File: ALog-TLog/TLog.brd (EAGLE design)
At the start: 124.1 x 45.3 mm, 94 parts, among them IC1 ATMEGA644M, J6 5.5x2.1mm Barrel, Q1 MOSFET-NCH-BSS138, Q5 MOSFET_PCH-IRLML2244, Q6 MOSFET_PCH-IRLML2244, Q7 MOSFET_PCH-IRLML2244, Q8 MOSFET-NCH-BSS138, Q9 MOSFET-NCH-BSS138, U2 FT231X-Q, U3 915MHz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

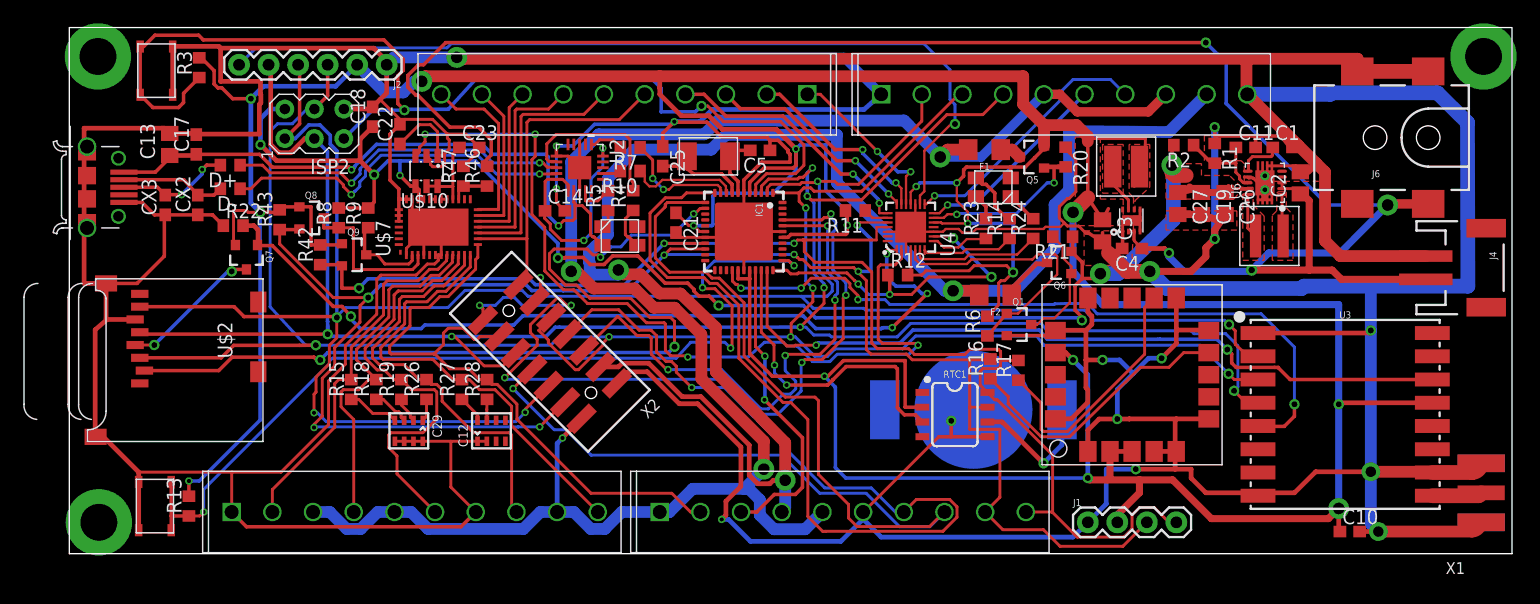
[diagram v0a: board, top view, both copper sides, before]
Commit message: Changes from round #1 of board testing
Changed capacitor sizes, fixed ADC COM pin, fixed DTR pin, connected 5V and VUSB, put converters in series, changed resistor divider values for switchmode regulator
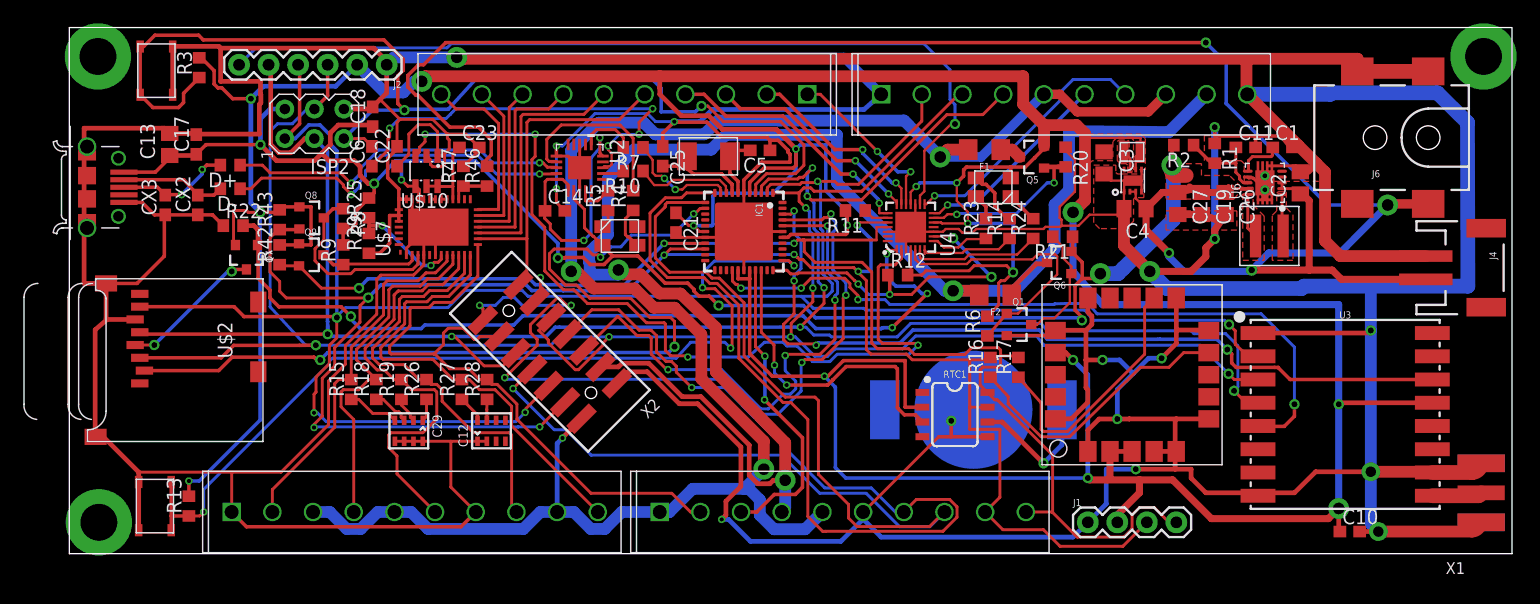
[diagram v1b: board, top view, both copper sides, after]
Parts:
- added C6: 0.1uF, bschulz:C0603
- added R25, R29: 10k, bschulz:R0603
- C4: device bschulz:C0603 -> bschulz:C0805
- L2: value 10uH -> 2.2uF; device bschulz:WE-LQS(4X4) -> bschulz:0806
- R1: value 143k -> 111k
- R2: value 953k -> 1M
- moved C3 5.84 mm to (89.2, 33.7)
- moved R9 3.84 mm to (23.7, 25.8)
- moved Q9 3.68 mm to (20.9, 25.8)
- moved R42 3.49 mm to (18.2, 25.8)
- moved C4 3.44 mm to (91.8, 29.8)
- moved U$4 3.43 mm to (91.6, 32.2)
- moved C22 1.92 mm to (28.3, 34.3)
- moved L2 1.37 mm to (91.6, 34.7)
- moved R8 0.39 mm to (23.7, 28.9), turned to 270 degrees
- moved R17 0.25 mm to (81.8, 16.1)
- moved R10 0.25 mm to (48.6, 33.0)
- moved R7 0.25 mm to (48.6, 35.1)
- moved R16 0.13 mm to (79.4, 16.1)
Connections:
- removed net VUSB: C13.1, C17.1, MICRO_USB.1, U$16.2, U2.12
- new net COM: R25.1, R29.2, U$7.7
- net 5V: now also C13.1, C17.1, C4.1, MICRO_USB.1, R25.2, U$16.2, U$4.2, U$4.3, U2.12
- net BATT+: no longer C4.1, U$4.2, U$4.3
- net DTR: now also C6.1
- net GND: now also R29.1; no longer U$7.7
- net RADIO_INT: now also IC1.42; no longer IC1.32
- net RST: now also C6.2
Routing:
- net VUSB: track 54.4 -> 0.00 mm, vias 2 -> 0
- net 5V: track 132.2 -> 176.4 mm, vias 8 -> 9
- net DTR: track 0.00 -> 35.6 mm, vias 0 -> 4
- net BATT+: track 161.4 -> 148.2 mm, vias 4 -> 3
- net COM: track 0.00 -> 9.61 mm, vias 0 -> 2
- net 3V3: track 429.8 -> 423.5 mm
- net RADIO_INT: track 65.9 -> 72.1 mm, vias 2 -> 4
- net GND: track 841.8 -> 847.5 mm
- net SDA: track 156.7 -> 160.0 mm
- net SDA_HV: track 13.5 -> 16.4 mm
- net RST: track 93.1 -> 95.8 mm
- net SCL: track 121.8 -> 124.3 mm
- net N$2: track 4.25 -> 1.75 mm
- net N$22: track 6.25 -> 8.31 mm
- net SD_VCC_CTRL: track 73.0 -> 75.0 mm
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
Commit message: Fixed Switchmode Converter Errors
Attempted to fix problems with switchmode 5v convetred by adding bottom layer ground plane, and generally improving top planes. In order to attempt to improve overall noise, analog plane was added. Also added control for PSYNC line on 5v converter to GPIO on IO expander
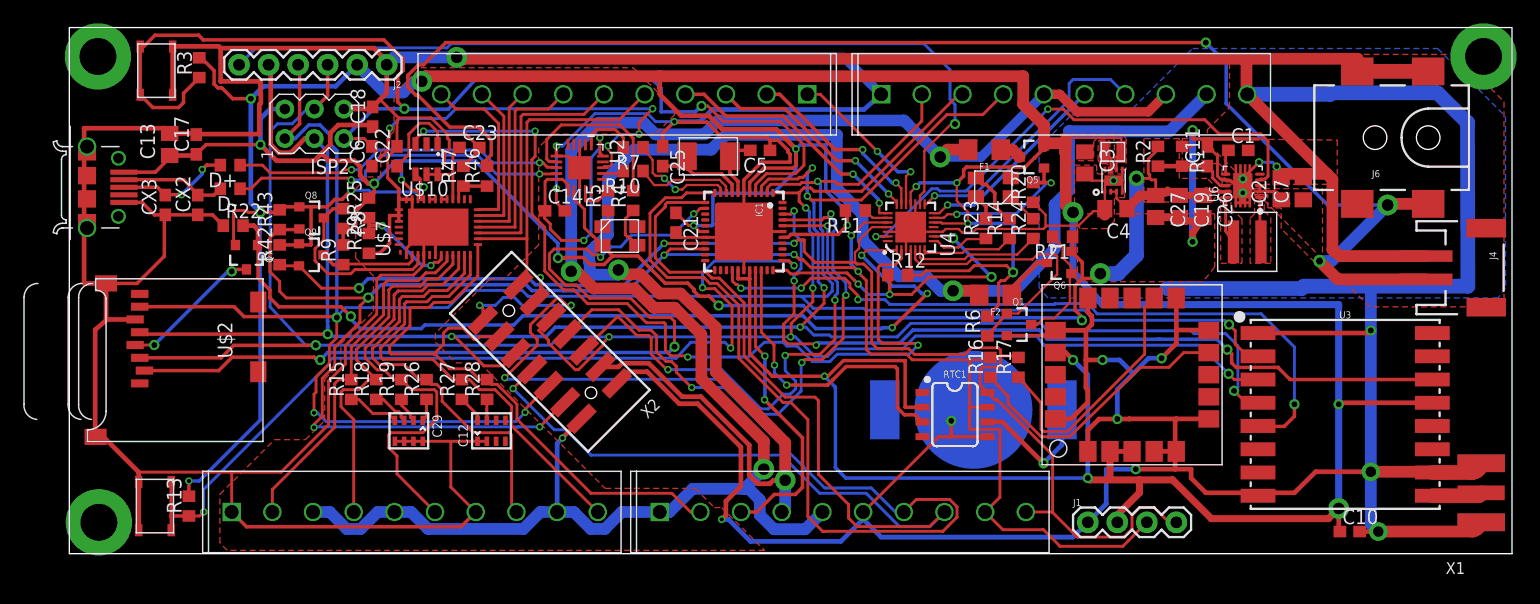
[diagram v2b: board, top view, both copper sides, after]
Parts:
- added C7: 10uF, bschulz:C0805
- moved R20 4.13 mm to (83.1, 31.2), turned to 90 degrees
- moved C1 3.82 mm to (100.7, 34.8)
- moved C11 3.39 mm to (98.0, 34.3), turned to 90 degrees
- moved R1 2.81 mm to (95.9, 34.3)
- moved R2 2.42 mm to (93.8, 34.3), turned to 90 degrees
- moved U$8 1.97 mm to (101.5, 26.9)
- moved C19 1.92 mm to (95.6, 30.0)
- moved C26 1.92 mm to (97.7, 30.0)
- moved C27 1.92 mm to (93.6, 30.0)
- moved U6 1.92 mm to (101.1, 31.8)
- moved C2 1.73 mm to (104.4, 31.5)
- moved C3 1.65 mm to (87.5, 33.7)
- moved C4 1.65 mm to (90.2, 29.8)
- moved L2 1.65 mm to (89.9, 34.7)
- moved U$4 1.65 mm to (90.0, 32.2)
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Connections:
- removed net BATT+: C2.1, J4.2, J6.VIN0, R46.2, U6.2, U6.3
- new net 5V_PSYNC: U4.27, U6.4
- new net BATT: C2.1, C7.1, J4.2, J6.VIN0, R46.2, U6.2, U6.3
- net 3V3: now also U$10.4
- net 5V: no longer U$10.4
- net GND: now also C7.2; no longer U6.4
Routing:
- net BATT+: track 148.2 -> 0.00 mm, vias 3 -> 0
- net BATT: track 0.00 -> 130.7 mm, vias 0 -> 3
- net 5V_PSYNC: track 0.00 -> 44.5 mm, vias 0 -> 2
- net GND: track 847.5 -> 830.9 mm, vias 16 -> 18
- net 5V: track 176.4 -> 161.9 mm, vias 9 -> 8
- net 3V3: track 423.5 -> 431.4 mm, vias 17 -> 19
- net SCL: track 124.3 -> 121.0 mm
- net SD_VCC_CTRL: track 75.0 -> 77.9 mm
- net N$4: track 3.87 -> 2.24 mm
- net EXT_5V: track 138.6 -> 140.1 mm
- net SDA: track 160.0 -> 158.7 mm
- net N$46: track 30.9 -> 29.6 mm
- net N$6: track 7.97 -> 6.86 mm
- net N$38: track 30.3 -> 29.2 mm
- net N$22: track 8.31 -> 7.40 mm
- added copper zone on layer 1, net BATT
- added copper zone on layer 16, net GND

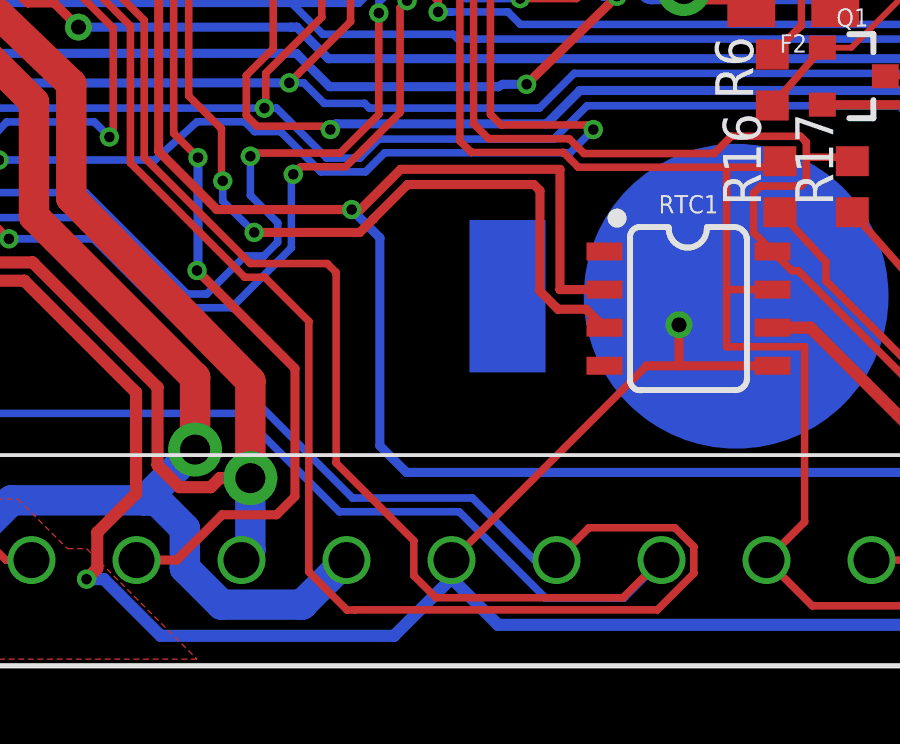
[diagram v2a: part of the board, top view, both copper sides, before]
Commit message: Changed part number for ATMEGA644P
Fixed the part and digikey numbers, was ATMEGA644A, now ATMEGA644PA
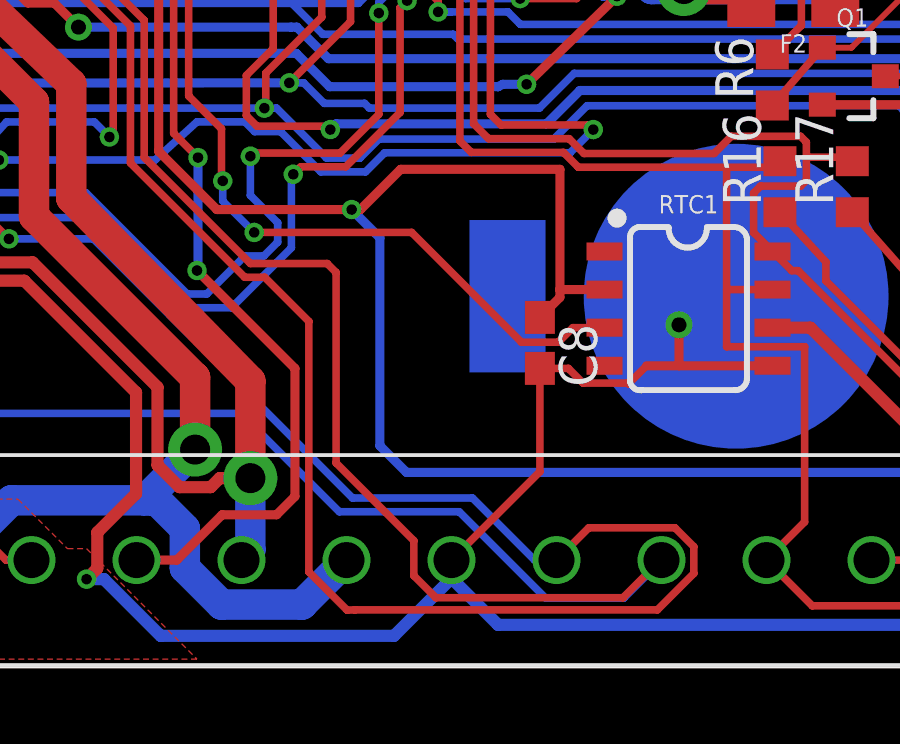
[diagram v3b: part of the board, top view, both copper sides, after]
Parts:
- added C8: (no value), bschulz:C0603
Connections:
- net 3V3: now also C8.1
- net GND: now also C8.2
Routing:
- net RTC_INT: track 27.1 -> 24.2 mm
- net GND: track 830.9 -> 833.3 mm
- net 3V3: track 431.4 -> 432.6 mm
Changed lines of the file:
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@@
 <?xml version="1.0" encoding="utf-8"?>
 <!DOCTYPE eagle SYSTEM "eagle.dtd">
-<eagle version="8.3.0">
+<eagle version="8.3.2">
 <drawing>
 <settings>
@@
 <attribute name="MPN" value="CL21A106KQCLRNC" x="106.299" y="31.496" size="1.778" layer="27" rot="R90" display="off"/>
 </element>
+<element name="C8" library="bschulz" package="C0603" value="" x="71.374" y="10.922" rot="R270">
+<attribute name="DIGIKEY" value="" x="71.374" y="10.922" size="1.778" layer="27" rot="R270" display="off"/>
+<attribute name="MF" value="" x="71.374" y="10.922" size="1.778" layer="27" rot="R270" display="off"/>
+<attribute name="MPN" value="" x="71.374" y="10.922" size="1.778" layer="27" rot="R270" display="off"/>
+</element>
 </elements>
 <signals>
@@
 <wire x1="98.132" y1="35.7806" x2="96.774" y2="35.7806" width="0.3048" layer="1"/>
 <wire x1="96.774" y1="35.7806" x2="96.774" y2="36.5426" width="0.3048" layer="1"/>
-<wire x1="74.92989375" y1="10.16" x2="68.45289375" y2="3.683" width="0.254" layer="1"/>
+<wire x1="74.326696875" y1="9.556803125" x2="74.92989375" y2="10.16" width="0.254" layer="1"/>
 <wire x1="68.45289375" y1="3.683" x2="68.427" y2="3.683" width="0.254" layer="1"/>
 <wire x1="11.049" y1="36.156" x2="10.949" y2="36.256" width="0.4064" layer="1"/>
@@
 <wire x1="27.948" y1="34.906240625" x2="28.321" y2="35.279240625" width="0.254" layer="1"/>
 <wire x1="27.5186" y1="34.22525625" x2="27.948" y2="34.65465625" width="0.254" layer="1"/>
+<contactref element="C8" pad="2"/>
+<wire x1="71.374" y1="10.072" x2="72.3232625" y2="10.072" width="0.254" layer="1"/>
+<wire x1="74.3005" y1="9.583" x2="74.326696875" y2="9.556803125" width="0.254" layer="1"/>
+<wire x1="72.3232625" y1="10.072" x2="72.8122625" y2="9.583" width="0.254" layer="1"/>
+<wire x1="72.8122625" y1="9.583" x2="74.3005" y2="9.583" width="0.254" layer="1"/>
+<wire x1="68.427" y1="3.683" x2="71.374" y2="6.63" width="0.254" layer="1"/>
+<wire x1="71.374" y1="6.63" x2="71.374" y2="10.072" width="0.254" layer="1"/>
 <wire x1="121.6025" y1="7.874" x2="121.6025" y2="7.874" width="0" layer="19" extent="1-16"/>
 <wire x1="121.6025" y1="2.794" x2="121.6025" y2="2.794" width="0" layer="19" extent="1-16"/>
@@
 <via x="61.849" y="14.605" extent="1-16" drill="0.35" shape="octagon"/>
 <via x="60.80125" y="16.3195" extent="1-16" drill="0.35" shape="octagon"/>
-<wire x1="73.527" y1="11.43" x2="72.9126" y2="12.0444" width="0.3048" layer="1"/>
-<wire x1="72.9126" y1="12.0444" x2="71.977925" y2="12.0444" width="0.3048" layer="1"/>
-<wire x1="71.977925" y1="12.0444" x2="71.374" y2="12.648325" width="0.3048" layer="1"/>
-<wire x1="71.374" y1="12.648325" x2="71.374" y2="16.002" width="0.3048" layer="1"/>
-<wire x1="71.374" y1="16.002" x2="71.17625" y2="16.19975" width="0.3048" layer="1"/>
-<wire x1="71.17625" y1="16.19975" x2="66.961865625" y2="16.19975" width="0.3048" layer="1"/>
 <contactref element="IC1" pad="31"/>
 <wire x1="60.80125" y1="16.3195" x2="60.76" y2="16.48775" width="0.254" layer="1"/>
@@
 <wire x1="60.80125" y1="16.3195" x2="60.80125" y2="15.65275" width="0.254" layer="16"/>
 <wire x1="60.80125" y1="15.65275" x2="61.849" y2="14.605" width="0.254" layer="16"/>
-<wire x1="66.961865625" y1="16.19975" x2="65.8306625" y2="15.068546875" width="0.3048" layer="1"/>
-<wire x1="65.8306625" y1="15.068546875" x2="65.8306625" y2="15.062725" width="0.3048" layer="1"/>
-<wire x1="65.8306625" y1="15.062725" x2="65.3729375" y2="14.605" width="0.3048" layer="1"/>
-<wire x1="65.3729375" y1="14.605" x2="61.849" y2="14.605" width="0.3048" layer="1"/>
+<wire x1="70.7592625" y1="10.945" x2="71.9887375" y2="10.945" width="0.254" layer="1"/>
+<wire x1="61.849" y1="14.605" x2="67.0992625" y2="14.605" width="0.254" layer="1"/>
+<wire x1="67.0992625" y1="14.605" x2="70.7592625" y2="10.945" width="0.254" layer="1"/>
+<wire x1="71.9887375" y1="10.945" x2="72.4737375" y2="11.43" width="0.254" layer="1"/>
+<wire x1="72.4737375" y1="11.43" x2="73.527" y2="11.43" width="0.254" layer="1"/>
 </signal>
 <signal name="LED1">
@@
 <via x="109.347" y="3.984625" extent="1-16" drill="1" shape="octagon"/>
 <wire x1="109.347" y1="12.954" x2="109.347" y2="3.984625" width="0.6096" layer="16"/>
-<wire x1="73.527" y1="12.7" x2="72.04075" y2="12.7" width="0.3048" layer="1"/>
+<wire x1="72.04075" y1="12.7" x2="73.527" y2="12.7" width="0.3048" layer="1"/>
 <contactref element="Q5" pad="2"/>
 <wire x1="108.457625" y1="3.1115" x2="109.347" y2="3.984625" width="0.6096" layer="1"/>
@@
 <wire x1="62.214609375" y1="27.565359375" x2="66.275859375" y2="27.565359375" width="0.3048" layer="1"/>
 <wire x1="66.275859375" y1="27.565359375" x2="67.06325" y2="28.35275" width="0.3048" layer="1"/>
+<contactref element="C8" pad="1"/>
+<wire x1="71.374" y1="11.772" x2="72.04075" y2="12.43875" width="0.3048" layer="1"/>
+<wire x1="72.04075" y1="12.43875" x2="72.04075" y2="12.7" width="0.3048" layer="1"/>
 </signal>
 <signal name="N$9">

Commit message: add gerber files and make some BOM improvements
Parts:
- added LOGO1: OSHW-LOGOM, SparkFun-Aesthetics:OSHW-LOGO-M
- added U$13: (no value), csandell:MN_SILK
- added U$3: NWLOGO_MED, awickert:NWLOGO_MED
- C18: value .1uF -> 0.1uF
- C25, C5: device rcl:C0603 -> bschulz:C0603
- U6: device bschulz:MICROBUILDER_PWSON-N10 -> bschulz:PWSON-N10
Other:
- board text added: "Developed in part at the University of Minnesota in parntnership with Northern Widget LLC"
- board text added: "Open-source for the outdoors"
- board text added: "TLog v1.0.0 ---------------------- Open-source scientific data logger ---------------------- Made in Minnesota"
- board text added: "TM"
